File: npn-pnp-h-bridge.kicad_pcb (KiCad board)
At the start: 2 copper layers, 45 x 19 mm, 35 parts, among them J1 S4B-PH-K-S_LF__SN_, J2 S2B-PH-K-S_LF__SN_, Q1 MMDT3904, Q2 MMDT3904

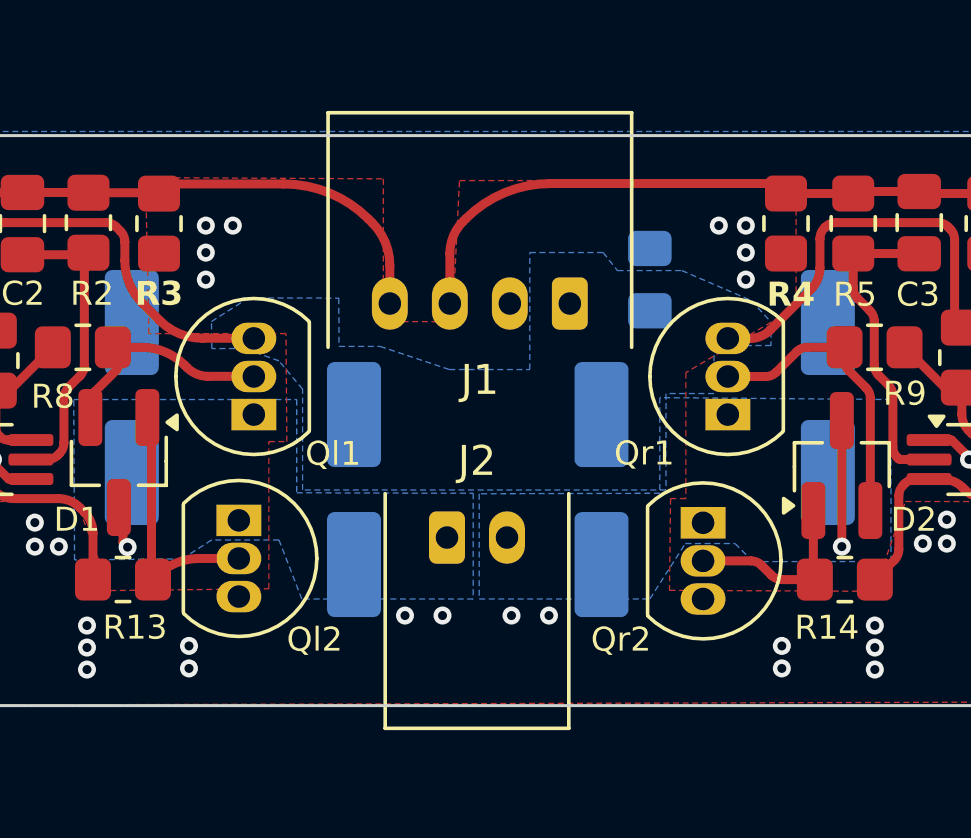
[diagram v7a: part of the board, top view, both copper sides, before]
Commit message: pushed out the connectors to match the case
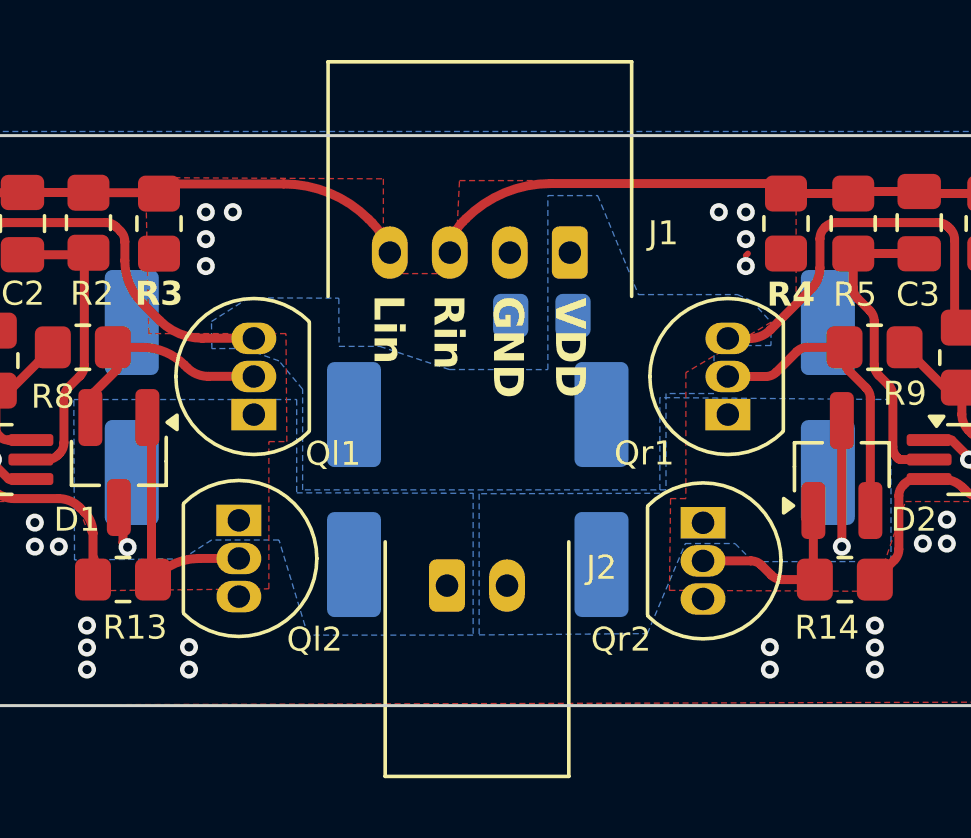
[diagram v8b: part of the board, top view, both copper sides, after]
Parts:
- moved C5 3.79 mm to (113.0, 55.6), turned to 180 degrees
- moved J1 1.70 mm to (113.9, 53.5)
- moved J2 1.60 mm to (109.8, 64.6)
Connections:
- net /H1b renamed /Hlb
- net /H2b renamed /Hrb
- net /L1b renamed /Llb
- net /L2b renamed /Lrb
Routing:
- net /R_IN: track 23.1 -> 21.4 mm
- net /L_IN: track 19.5 -> 18.2 mm
- net GND: vias 30 -> 26
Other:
- board text added: "Lin"
- board text added: "Rin"
- board text removed: "L_in"
- board text removed: "R_in"
